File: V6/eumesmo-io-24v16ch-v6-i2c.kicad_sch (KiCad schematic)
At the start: 24 parts, among them J9 250-203, SW2 1WIRE_SEL, U10 MCP23017, U11 DS2482S-100, U8 MCP23008, U9 MCP23008

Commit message: Replaced 0603 10k resistors for 0805.
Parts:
- C26, D10, D9, J9, R37, R38, SW2, U10, U11, U8, U9: FT Rotation Offset (none) -> 0; JLCPCB BOM 1 -> (none)
- C27: renamed from C29; FT Rotation Offset (none) -> 0; JLCPCB BOM 1 -> (none)
- C28: renamed from C33; FT Rotation Offset (none) -> 0; JLCPCB BOM 1 -> (none)
- C29: renamed from C34; FT Rotation Offset (none) -> 0; JLCPCB BOM 1 -> (none)
- C30: renamed from C31; FT Rotation Offset (none) -> 0; JLCPCB BOM 1 -> (none)
- C31: renamed from C32; FT Rotation Offset (none) -> 0; JLCPCB BOM 1 -> (none)
- C32: renamed from C27; FT Rotation Offset (none) -> 0; JLCPCB BOM 1 -> (none)
- C33: renamed from C28; FT Rotation Offset (none) -> 0; JLCPCB BOM 1 -> (none)
- C34: renamed from C30; FT Rotation Offset (none) -> 0; JLCPCB BOM 1 -> (none)
- R39: renamed from R41; FT Rotation Offset (none) -> 0; JLCPCB BOM 1 -> (none)
- R40: value 1k8/125mW -> 1,8k/125mW; FT Rotation Offset (none) -> 0; JLCPCB BOM 1 -> (none)
- R41: renamed from R39; FT Rotation Offset (none) -> 0; JLCPCB BOM 1 -> (none)
- TP14: renamed from TP16; value SDA -> TP; JLCPCB BOM 0 -> (none); now not fitted; now left out of the parts list
- TP15: renamed from TP17; value SCL -> TP; JLCPCB BOM 0 -> (none); now not fitted; now left out of the parts list

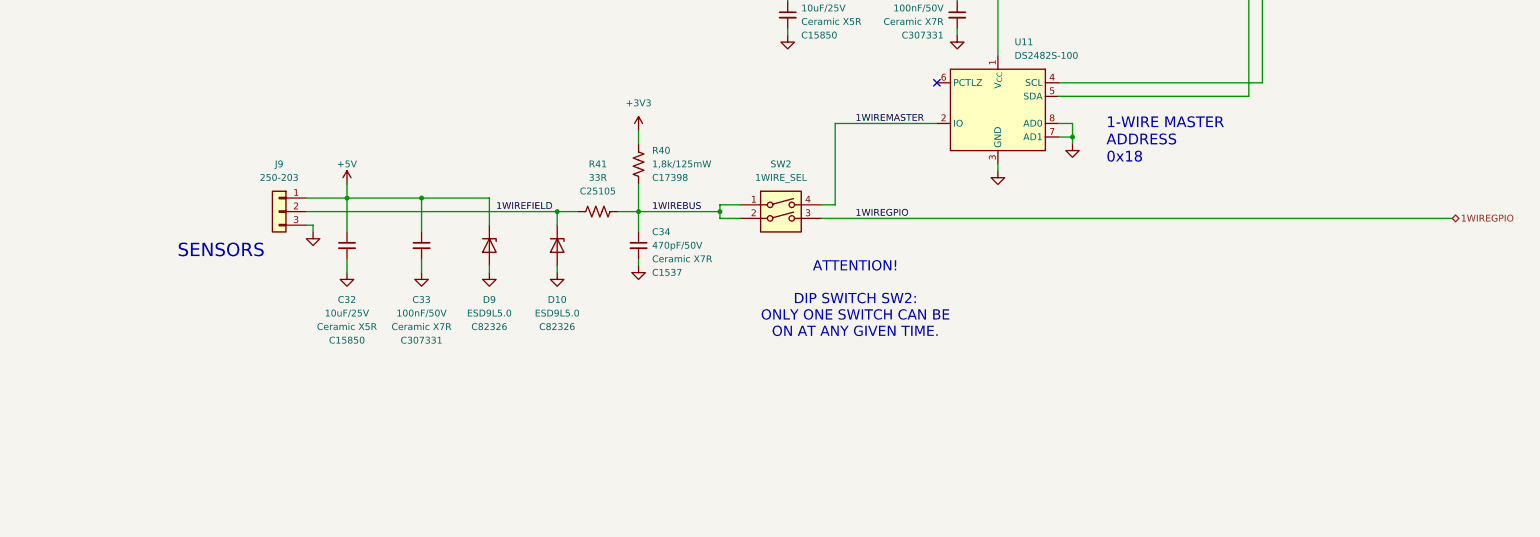
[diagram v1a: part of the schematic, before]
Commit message: Added jumper to 1-wire interface
The jumper JP1 must be closed to connect the 1-wire input to GPIO16 when the dip switch and the 1-wire master IC are not installed.
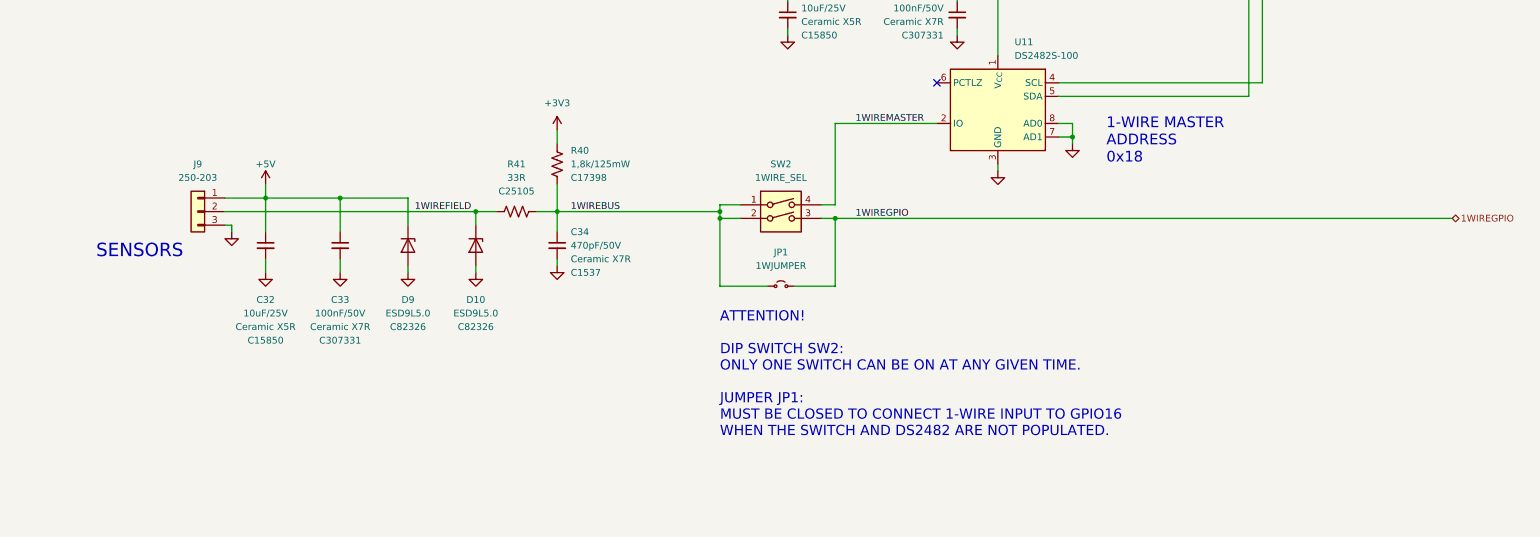
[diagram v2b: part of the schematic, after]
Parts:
- added JP1: 1WJUMPER, Jumper:SolderJumper-2_P1.3mm_Open_RoundedPad1.0x1.5mm, symbol Jumper:Jumper_2_Small_Open
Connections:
- net 1WIREBUS: now also JP1.1 (A)
- net 1WIREGPIO: now also JP1.2 (B)
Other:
- note added: "ATTENTION! DIP SWITCH SW2: ONLY ONE SWITCH CAN BE ON AT ANY GIVEN TIME. JUMPER JP1: MUST BE CLOSED TO CONNECT 1-WIRE INPUT TO GPIO16 WHEN THE SWITCH AND DS2482 ARE NOT POPULATED."
- note removed: "ATTENTION! DIP SWITCH SW2: ONLY ONE SWITCH CAN BE ON AT ANY GIVEN TIME."
- moved on the sheet: C32, C33, C34, D10, D9, J9, R40, R41
